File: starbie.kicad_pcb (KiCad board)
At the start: 2 copper layers, 7 parts, among them J1 Conn_01x04_Pin, J2 Conn_01x08_Pin, SW1 SW_Push, SW2 SW_Push, U1 XIAO-ESP32-C3-SMD, U2 DHT11

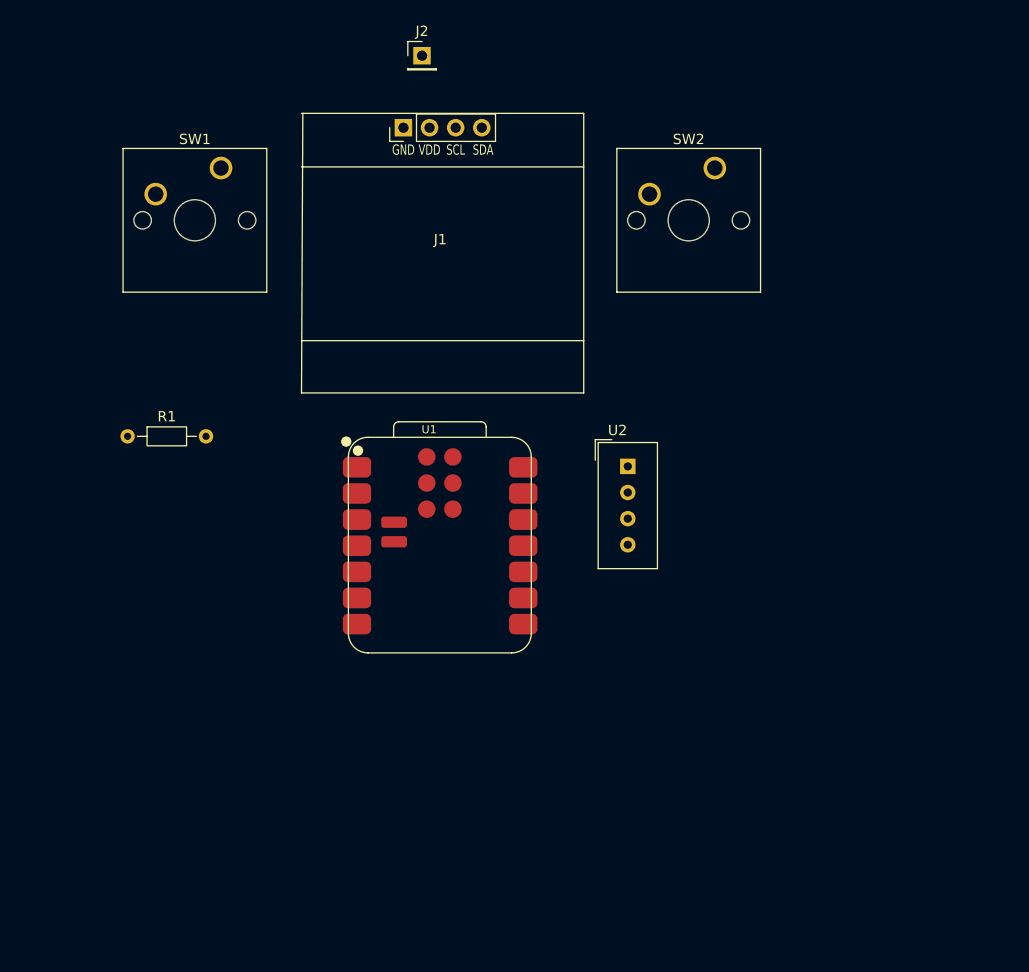
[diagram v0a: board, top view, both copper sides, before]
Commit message: Addeded BOM fixed stuff and added decorations
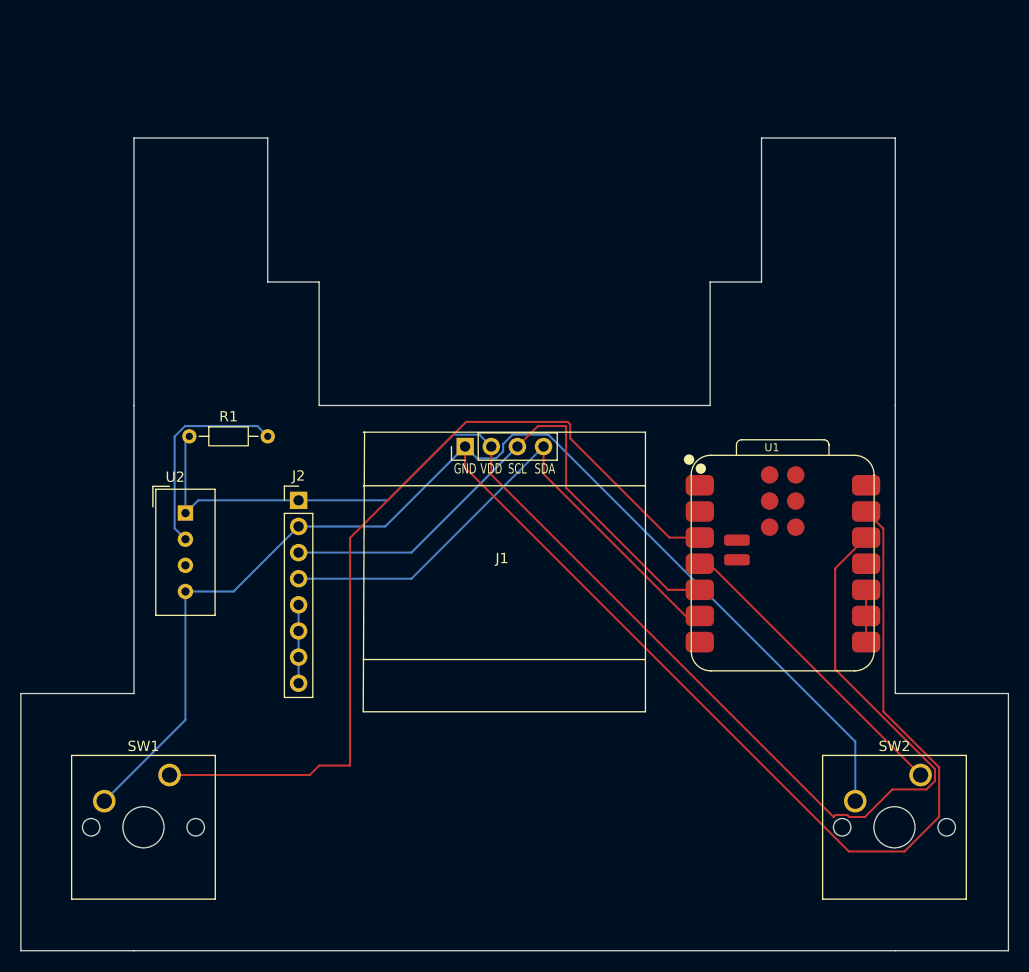
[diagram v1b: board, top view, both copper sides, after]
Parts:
- J2: footprint Connector_PinHeader_2.54mm:PinHeader_1x01_P2.54mm_Vertical -> Connector_PinHeader_2.54mm:PinHeader_1x08_P2.54mm_Vertical
- moved SW2 62.3 mm to (178.5, 94.9)
- moved SW1 59.2 mm to (105.5, 94.9)
- moved J2 44.9 mm to (118.0, 68.2)
- moved U2 43.2 mm to (107.0, 69.5)
- moved U1 33.4 mm to (156.2, 84.9)
- moved J1 31.6 mm to (138.0, 63.0)
- moved R1 6.00 mm to (107.4, 62.0)
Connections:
- R1 pad 2: /DH11 DATA -> /DHT11 DATA
- SW2 pad 1: /GPIO1 -> /GPIO3
- U1 pad 1: unconnected-(U1-D0-Pad1) -> /X
- U1 pad 2: unconnected-(U1-D1-Pad2) -> /DHT11 DATA
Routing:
- net GND: track 0.00 -> 212.2 mm
- net +3.3V: track 0.00 -> 131.2 mm
- net /GPIO2: track 0.00 -> 84.2 mm
- net /SCL: track 0.00 -> 54.2 mm
- net /SDA: track 0.00 -> 52.7 mm
- net /GPIO3: track 0.00 -> 30.0 mm
- net /DHT11 DATA: track 0.00 -> 20.3 mm
- net /X: track 0.00 -> 12.7 mm
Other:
- board outline added: 96 x 79 mm

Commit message: Generated gerbers and added firmware
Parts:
- added G***: LOGO, LOGO, F.Cu at (157.0, 97.0)
- added G***: LOGO, LOGO, F.Cu at (144.0, 97.0)

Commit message: Added new Gerbers
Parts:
- moved J1 1.04 mm to (138.3, 64.0)
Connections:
- J2 pad 5: /X -> unconnected-(J2-Pin_5-Pad5)
- J2 pad 6: /X -> unconnected-(J2-Pin_6-Pad6)
- J2 pad 7: /X -> unconnected-(J2-Pin_7-Pad7)
- J2 pad 8: /X -> unconnected-(J2-Pin_8-Pad8)
- U1 pad 1: /X -> unconnected-(U1-D0-Pad1)
- U1 pad 10: /X -> unconnected-(U1-D9/BOOT-Pad10)
- U1 pad 18: unconnected-(U1-GND-Pad18) -> GND
- U1 pad 7: /X -> unconnected-(U1-D6-Pad7)
- U1 pad 8: /X -> unconnected-(U1-D7-Pad8)
- U1 pad 9: /X -> unconnected-(U1-D8-Pad9)
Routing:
- net /SDA: track 52.7 -> 170.8 mm
- net /SCL: track 54.2 -> 157.3 mm
- net /DHT11 DATA: track 20.3 -> 107.7 mm
- net +3.3V: track 131.2 -> 87.2 mm
- net GND: track 212.2 -> 180.2 mm
- net /GPIO2: track 84.2 -> 70.3 mm
- net /X: track 12.7 -> 0.00 mm
- net /GPIO3: track 30.0 -> 37.8 mm
